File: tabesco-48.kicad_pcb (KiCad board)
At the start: 2 copper layers, 289.3 x 95.2 mm, 142 parts, among them J0 AVR-ISP-6, J1 Conn_01x04, SW0 SW_Push, U1 ATmega32U4-A, U2 SRV05-4, Y0 16MHz

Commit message: prepping for kicanvas
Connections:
- R0 pad 2: Net-(U1-~{RESET}) -> RST
- SW0 pad 2: Net-(U1-~{RESET}) -> RST
- U1 pad 13: Net-(U1-~{RESET}) -> RST
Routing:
- net RST: track 0.00 -> 41.2 mm, vias 0 -> 1
- net Net-(U1-~{RESET}): track 32.2 -> 0.00 mm, vias 1 -> 0
- net GND: track 144.3 -> 162.6 mm, vias 3 -> 5
- net SCK: track 18.3 -> 17.2 mm
- net /col5: track 133.7 -> 132.6 mm, vias 2 -> 0
- net /col9: track 184.1 -> 185.1 mm, vias 2 -> 0
- net /col6: track 153.3 -> 152.3 mm, vias 2 -> 0
- net MISO: track 14.8 -> 14.0 mm
- net /row2: track 281.7 -> 282.4 mm, vias 0 -> 2
- net /row1: track 314.8 -> 314.1 mm, vias 2 -> 6
- net /col4: track 142.8 -> 143.5 mm, vias 2 -> 0
- net /col10: track 224.6 -> 225.2 mm, vias 2 -> 0
- net D-: track 24.6 -> 24.0 mm, vias 2 -> 0
- net /row0: track 346.2 -> 345.7 mm, vias 2 -> 6
- net VBUS: track 27.3 -> 27.6 mm, vias 0 -> 2
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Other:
- board size 289.3 x 95.2 mm -> 294.1 x 100 mm

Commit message: more prep 4 kicanvas
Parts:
- moved C0 302.1 mm to (198.9, 139.3)
- moved C1 302.1 mm to (183.0, 140.7)
- moved D11 302.1 mm to (344.9, 114.2)
- moved D13 302.1 mm to (108.0, 133.3)
- moved D14 302.1 mm to (127.0, 133.3)
- moved D15 302.1 mm to (146.1, 133.3)
- moved D16 302.1 mm to (165.1, 133.3)
- moved D17 302.1 mm to (199.6, 133.3)
- moved D18 302.1 mm to (221.1, 133.3)
- moved D19 302.1 mm to (240.1, 133.3)
- moved D20 302.1 mm to (259.2, 133.3)
- moved D21 302.1 mm to (278.2, 133.3)
- moved D22 302.1 mm to (297.3, 133.3)
- moved D23 302.1 mm to (316.3, 133.3)
- moved D24 302.1 mm to (335.4, 133.3)
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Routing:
- added copper zone on B.Cu, net GND
- added copper zone on F.Cu, net GND

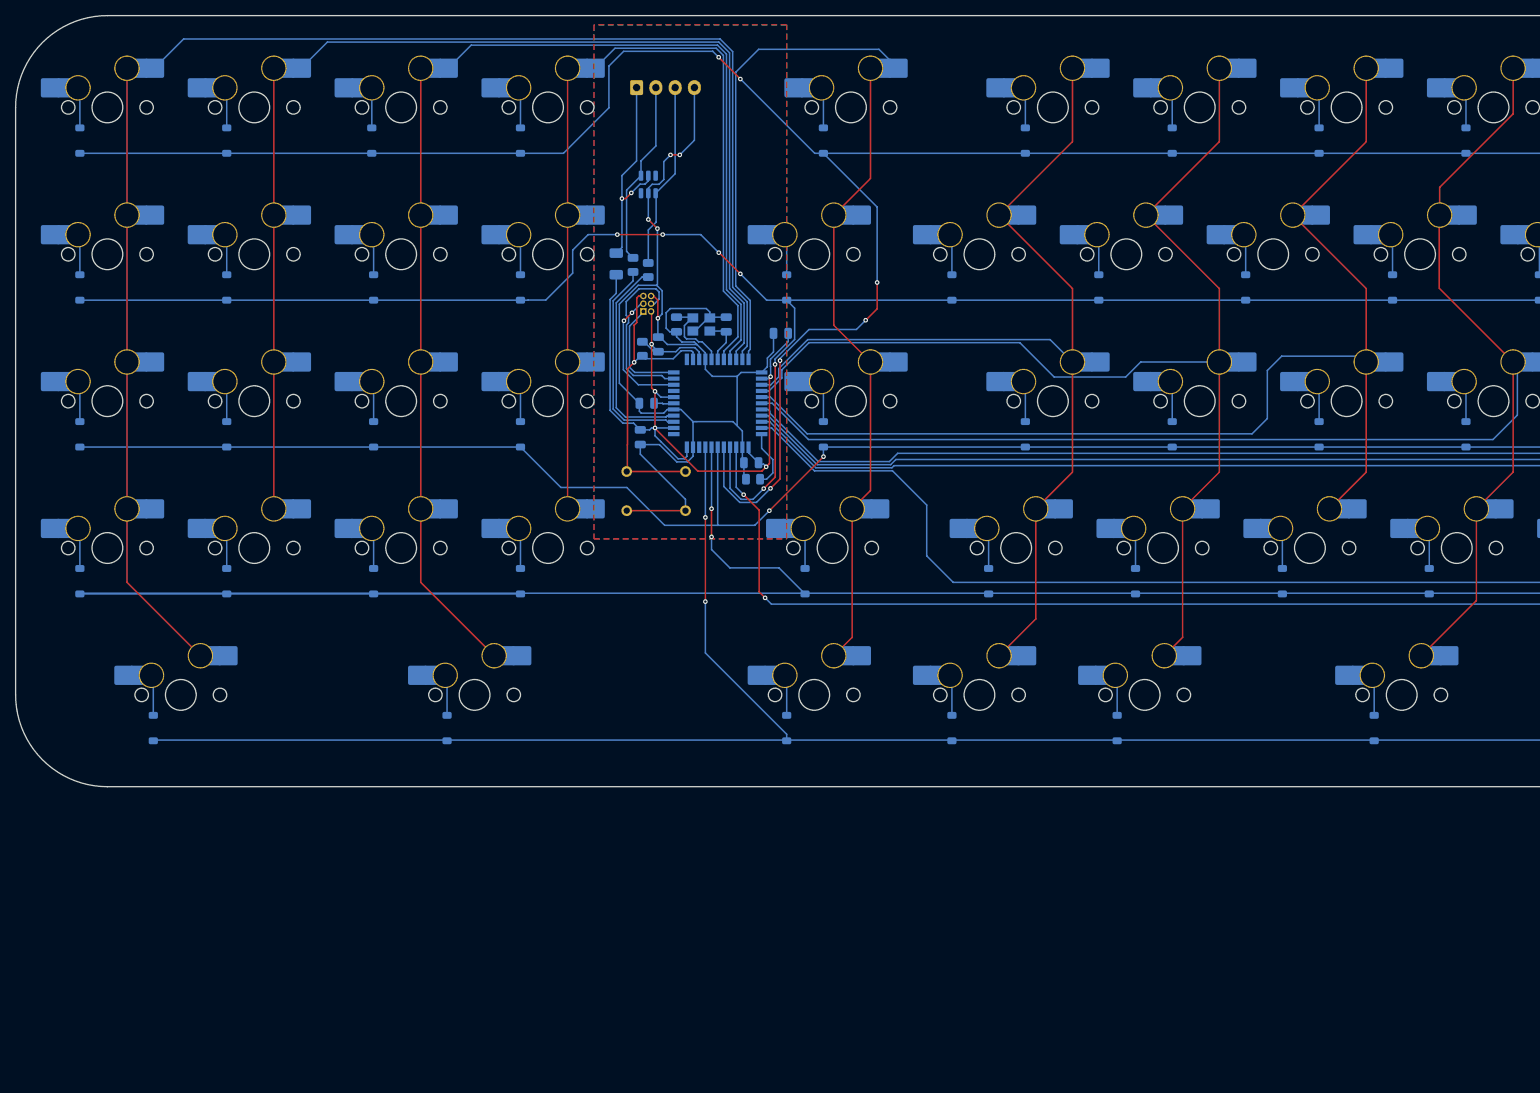
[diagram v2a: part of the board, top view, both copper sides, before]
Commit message: fixed(?) UDB connector, some GND fill work
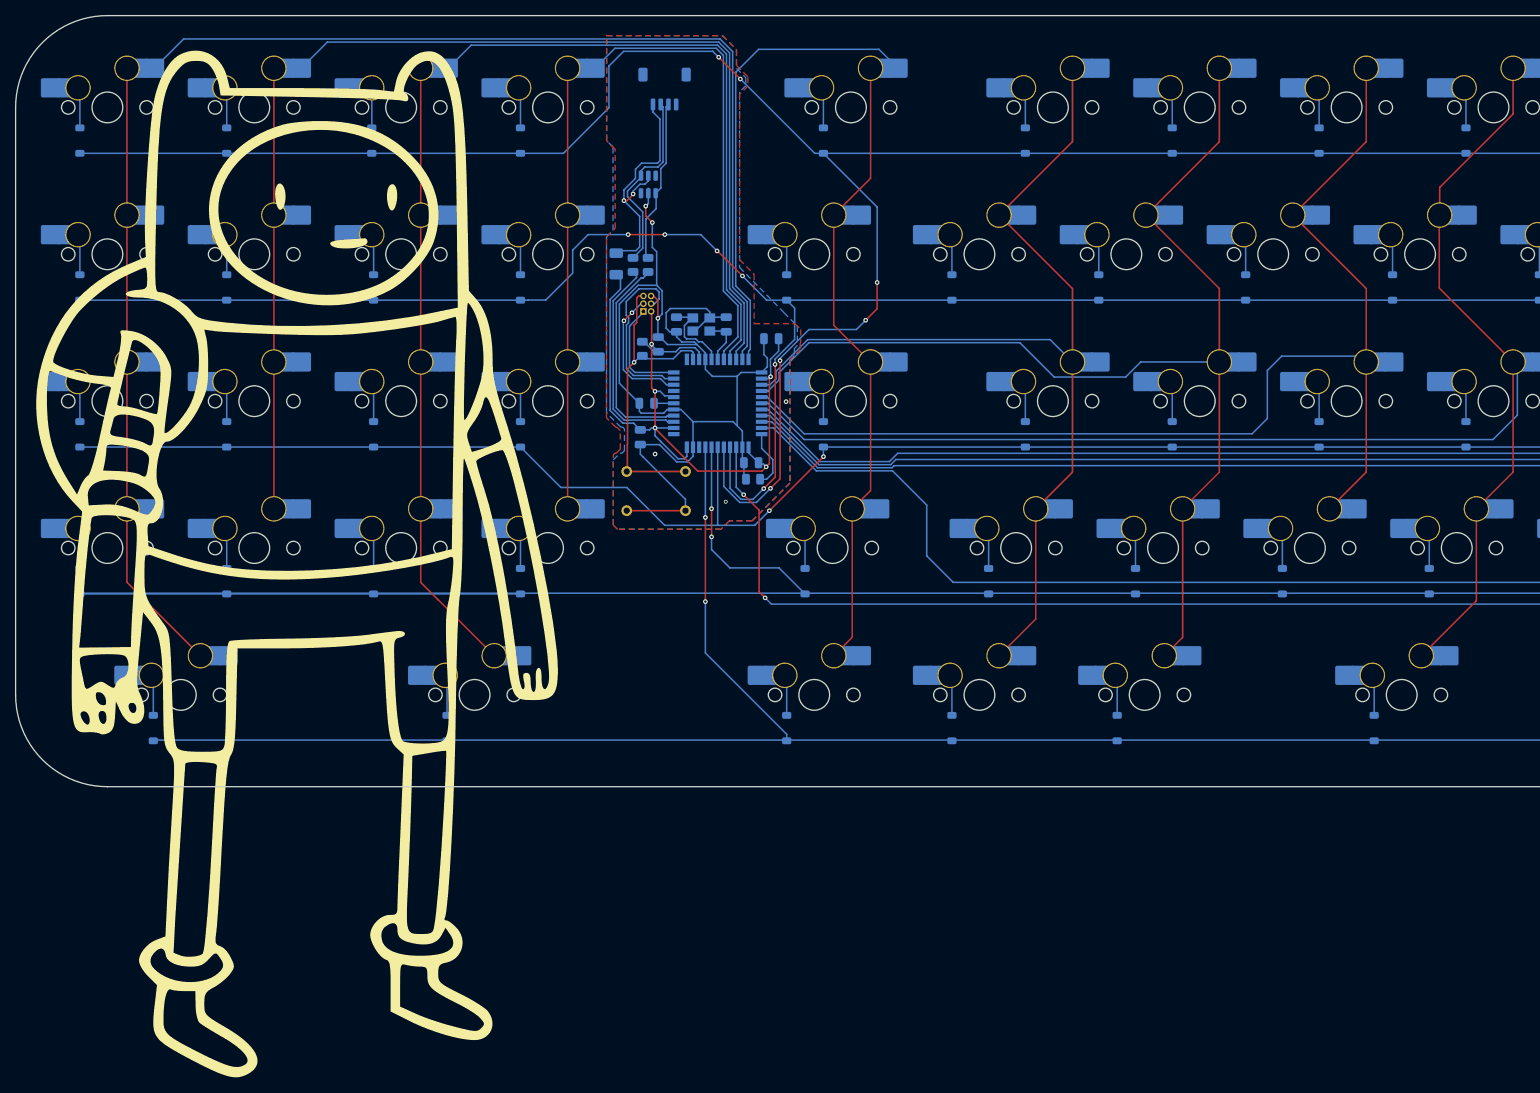
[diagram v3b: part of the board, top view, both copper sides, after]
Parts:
- J1: footprint Connector_JST:JST_EH_S4B-EH_1x04_P2.50mm_Horizontal -> Connector_JST:JST_SH_SM04B-SRSS-TB_1x04-1MP_P1.00mm_Horizontal
- moved J1 3.63 mm to (183.8, 107.6)
- moved C0 1.42 mm to (197.6, 139.9)
- moved R1 0.66 mm to (181.7, 130.4)
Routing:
- net GND: track 162.6 -> 145.2 mm, vias 5 -> 6
- net VBUS: track 27.6 -> 31.4 mm
- net D+: track 24.2 -> 21.3 mm
- net +5V: track 104.4 -> 103.6 mm

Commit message: sch/pcb adjustments (UDB)
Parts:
- removed F0: 500mA, Fuse:Fuse_1206_3216Metric
- removed U2: SRV05-4, Package_TO_SOT_SMD:SOT-23-6
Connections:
- J1 pad 1: VBUS -> +5V
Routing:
- net GND: track 145.2 -> 101.4 mm, vias 6 -> 3
- net VBUS: track 31.4 -> 0.00 mm, vias 2 -> 0
- net +5V: track 103.6 -> 126.9 mm
- net D-: track 24.3 -> 21.6 mm
- net Net-(U1-D+): track 27.5 -> 26.8 mm

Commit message: BOM/CPL generated
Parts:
- moved R1 17.2 mm to (178.5, 147.3)
- moved R2 17.2 mm to (176.6, 147.3)
- moved J1 12.0 mm to (182.1, 119.5)
- moved C6 0.46 mm to (181.9, 148.3)
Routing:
- net Net-(U1-D+): track 26.8 -> 8.99 mm
- net Net-(U1-D-): track 27.5 -> 9.67 mm
- net +5V: track 126.9 -> 117.2 mm
- net D+: track 21.6 -> 27.2 mm
- net D-: track 21.6 -> 27.2 mm
- net /col4: track 143.5 -> 147.1 mm
- net /col2: track 158.9 -> 156.4 mm
- net /col1: track 155.6 -> 153.1 mm
- net /col3: track 116.2 -> 113.7 mm
- net /col0: track 198.4 -> 195.8 mm
- net /col11: track 225.5 -> 227.6 mm
- net /col8: track 197.5 -> 199.5 mm
- net /col9: track 185.0 -> 187.0 mm
- net /col10: track 225.2 -> 227.0 mm
- net GND: track 101.4 -> 100.0 mm
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
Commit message: reorganized idk
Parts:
- MX12, MX31, MX39, MX4: footprint marbastlib-mx:SW_MX_HS_CPG151101S11_1u -> marbastlib-mx:SW_MX_HS_CPG151101S11_1.75u
- MX17, MX26, MX55, MX57: footprint marbastlib-mx:SW_MX_HS_CPG151101S11_1u -> marbastlib-mx:SW_MX_HS_CPG151101S11_1.25u
- MX44: footprint marbastlib-mx:SW_MX_HS_CPG151101S11_1u -> marbastlib-mx:SW_MX_HS_CPG151101S11_1.5u
- moved J1 61.8 mm to (192.2, 58.5)
- moved D2 47.5 mm to (154.5, 67.6)
- moved D29 47.5 mm to (154.5, 105.7)
- moved D42 47.5 mm to (154.5, 124.7)
- moved D54 47.5 mm to (164.1, 143.8)
- moved D0 47.5 mm to (116.4, 67.6)
- moved D1 47.5 mm to (135.5, 67.6)
- moved D15 47.5 mm to (154.5, 86.6)
- moved D27 47.5 mm to (116.4, 105.7)
- moved D28 47.5 mm to (135.5, 105.7)
- moved D3 47.5 mm to (173.6, 67.6)
- moved D30 47.5 mm to (173.6, 105.7)
- moved D40 47.5 mm to (116.4, 124.7)
- moved D41 47.5 mm to (135.5, 124.7)
- moved D43 47.5 mm to (173.6, 124.7)
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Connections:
- U1 pad 18: /col3 -> /row0
- U1 pad 19: /col2 -> /row1
- U1 pad 20: /col1 -> /row2
- U1 pad 21: /col0 -> /row4
- U1 pad 22: /col4 -> /row3
- U1 pad 25: /col5 -> /col13
- U1 pad 26: /col6 -> /col12
- U1 pad 27: /col7 -> /col11
- U1 pad 28: /col8 -> /col10
- U1 pad 30: /col10 -> /col6
- U1 pad 31: /col11 -> /col7
- U1 pad 32: /col12 -> /col8
- U1 pad 36: /col13 -> /col4
- U1 pad 37: /row1 -> /col5
- U1 pad 38: /row0 -> /col0
- U1 pad 39: /row2 -> /col1
- U1 pad 40: /row3 -> /col2
- U1 pad 41: /row4 -> /col3
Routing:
- net /row3: track 346.3 -> 263.6 mm
- net /col0: track 195.8 -> 146.8 mm, vias 0 -> 1
- net D-: track 27.2 -> 63.0 mm
- net D+: track 27.2 -> 63.0 mm
- net GND: track 100.0 -> 65.1 mm, vias 3 -> 8
- net +5V: track 117.2 -> 150.4 mm, vias 5 -> 7
- net /col4: track 147.1 -> 115.1 mm, vias 0 -> 1
- net Net-(U1-D+): track 8.99 -> 38.5 mm
- net Net-(U1-D-): track 9.67 -> 39.0 mm
- net /col1: track 153.1 -> 126.4 mm, vias 0 -> 1
- net /row4: track 304.2 -> 279.5 mm
- net /col2: track 156.4 -> 133.3 mm, vias 0 -> 2
- net /row0: track 345.9 -> 323.8 mm, vias 6 -> 2
- net RST: track 41.2 -> 61.5 mm, vias 1 -> 2
- net /col3: track 113.7 -> 132.7 mm, vias 0 -> 1
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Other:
- board size 294.1 x 100 mm -> 285 x 95.2 mm
